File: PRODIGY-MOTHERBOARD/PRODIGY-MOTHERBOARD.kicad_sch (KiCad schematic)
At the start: 0 parts

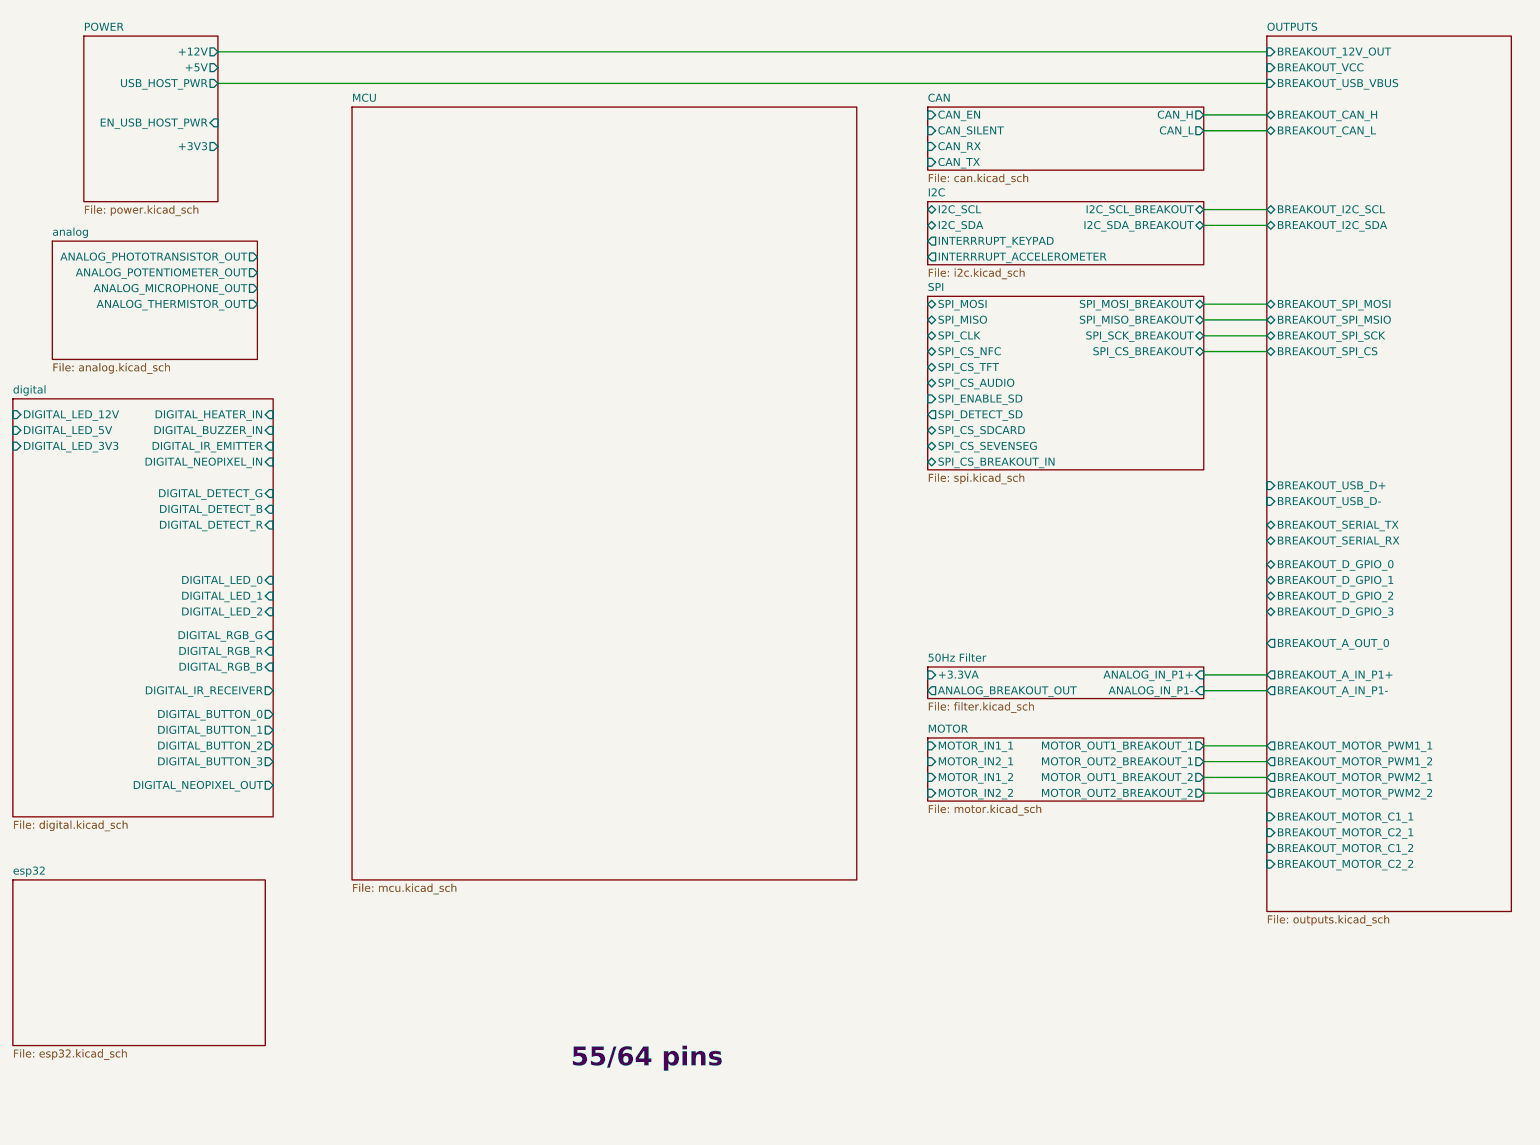
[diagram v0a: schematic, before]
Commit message: 2-axis joystick footprint and sybmbol created. Analog-side done.
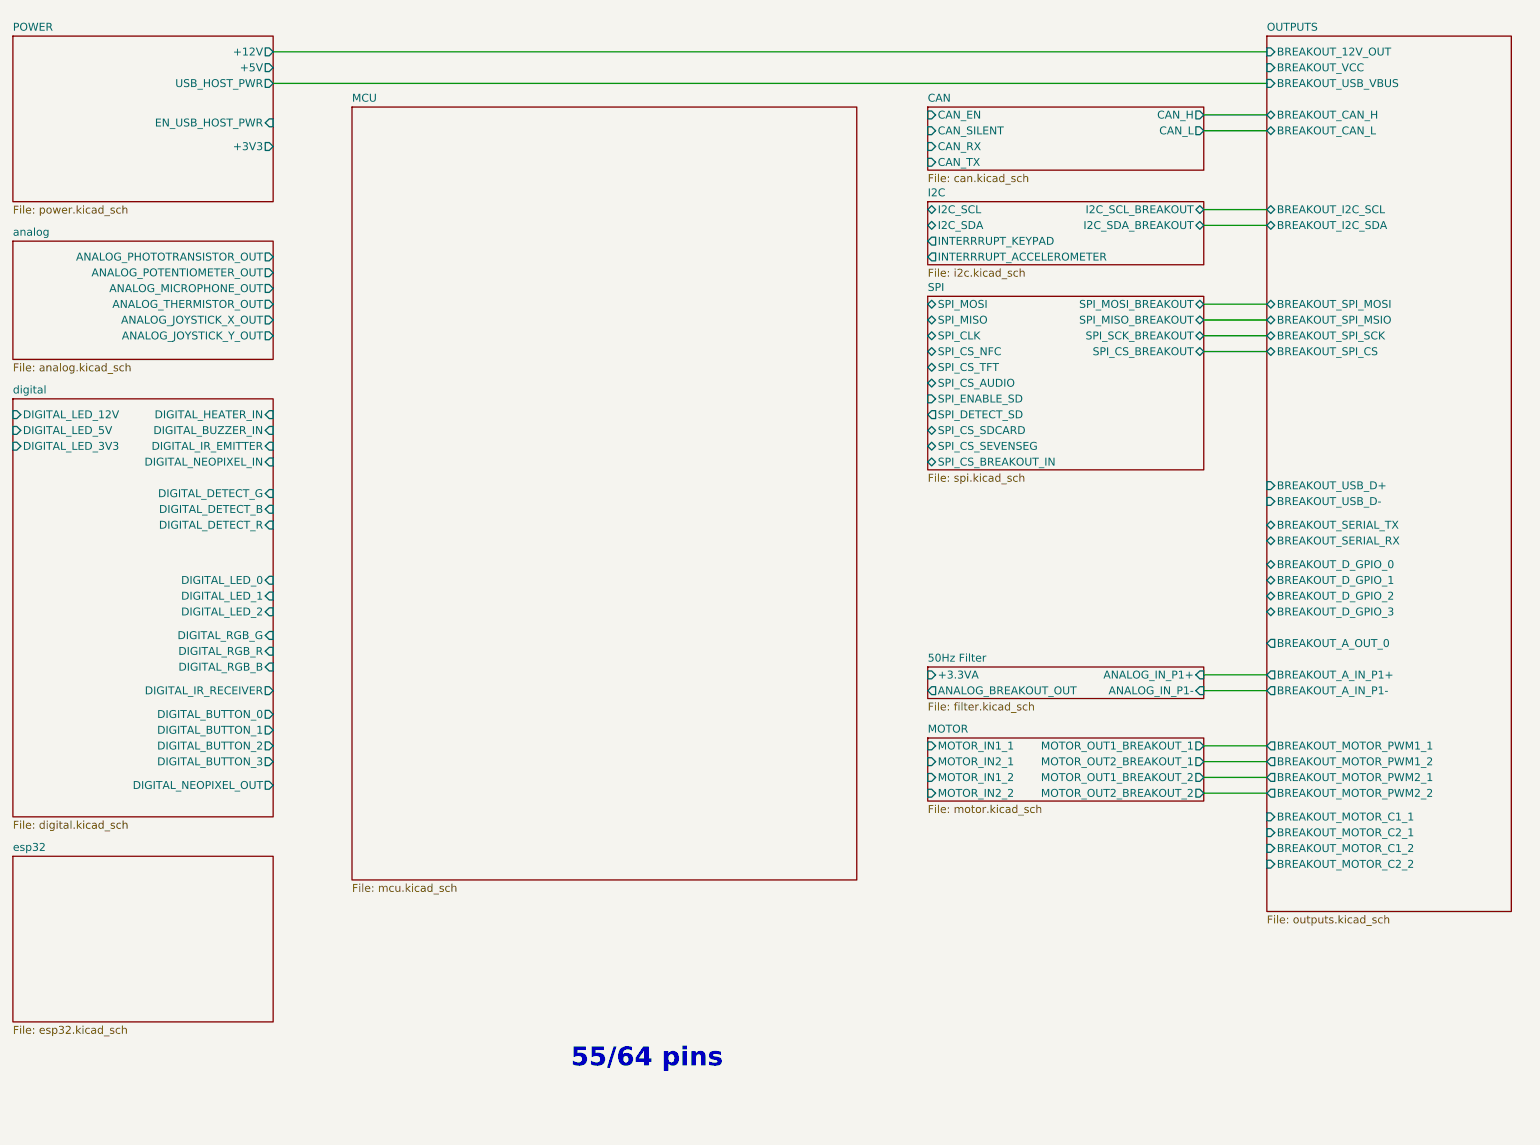
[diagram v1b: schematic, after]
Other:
- sheet analog ports: added ANALOG_JOYSTICK_X_OUT, ANALOG_JOYSTICK_Y_OUT; removed none
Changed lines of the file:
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@@
 	(wire
 		(pts
-			(xy 60.96 21.59) (xy 229.87 21.59)
+			(xy 69.85 21.59) (xy 229.87 21.59)
 		)
 		(stroke
@@
 	(wire
 		(pts
-			(xy 60.96 26.67) (xy 229.87 26.67)
+			(xy 69.85 26.67) (xy 229.87 26.67)
 		)
 		(stroke
@@
 	)
 	(sheet
-		(at 27.94 154.94)
-		(size 40.64 26.67)
+		(at 27.94 151.13)
+		(size 41.91 26.67)
 		(fields_autoplaced yes)
 		(stroke
@@
 		)
 		(property "Sheetname" "esp32"
-			(at 27.94 154.2284 0)
+			(at 27.94 150.4184 0)
 			(effects
 				(font
@@
 		)
 		(property "Sheetfile" "esp32.kicad_sch"
-			(at 27.94 182.1946 0)
+			(at 27.94 178.3846 0)
 			(effects
 				(font
@@
 		)
 		(property "Field2" ""
-			(at 27.94 154.94 0)
+			(at 27.94 151.13 0)
 			(effects
 				(font
@@
 	)
 	(sheet
-		(at 39.37 19.05)
-		(size 21.59 26.67)
+		(at 27.94 19.05)
+		(size 41.91 26.67)
 		(fields_autoplaced yes)
 		(stroke
@@
 		)
 		(property "Sheetname" "POWER"
-			(at 39.37 18.3384 0)
+			(at 27.94 18.3384 0)
 			(effects
 				(font
@@
 		)
 		(property "Sheetfile" "power.kicad_sch"
-			(at 39.37 46.3046 0)
+			(at 27.94 46.3046 0)
 			(effects
 				(font
@@
 		)
 		(pin "+3V3" output
-			(at 60.96 36.83 0)
+			(at 69.85 36.83 0)
 			(effects
 				(font
@@
 		)
 		(pin "+12V" output
-			(at 60.96 21.59 0)
+			(at 69.85 21.59 0)
 			(effects
 				(font
@@
 		)
 		(pin "+5V" output
-			(at 60.96 24.13 0)
+			(at 69.85 24.13 0)
 			(effects
 				(font
@@
 		)
 		(pin "USB_HOST_PWR" output
-			(at 60.96 26.67 0)
+			(at 69.85 26.67 0)
 			(effects
 				(font
@@
 		)
 		(pin "EN_USB_HOST_PWR" input
-			(at 60.96 33.02 0)
+			(at 69.85 33.02 0)
 			(effects
 				(font
@@
 	)
 	(sheet
-		(at 34.29 52.07)
-		(size 33.02 19.05)
+		(at 27.94 52.07)
+		(size 41.91 19.05)
 		(fields_autoplaced yes)
 		(stroke
@@
 		)
 		(property "Sheetname" "analog"
-			(at 34.29 51.3584 0)
+			(at 27.94 51.3584 0)
 			(effects
 				(font
@@
 		)
 		(property "Sheetfile" "analog.kicad_sch"
-			(at 34.29 71.7046 0)
+			(at 27.94 71.7046 0)
 			(effects
 				(font
@@
 		)
 		(property "Field2" ""
-			(at 34.29 52.07 0)
+			(at 27.94 52.07 0)
 			(effects
 				(font
@@
 		)
 		(pin "ANALOG_POTENTIOMETER_OUT" output
-			(at 67.31 57.15 0)
+			(at 69.85 57.15 0)
 			(effects
 				(font
@@
 		)
 		(pin "ANALOG_THERMISTOR_OUT" output
-			(at 67.31 62.23 0)
+			(at 69.85 62.23 0)
 			(effects
 				(font
@@
 		)
 		(pin "ANALOG_PHOTOTRANSISTOR_OUT" output
-			(at 67.31 54.61 0)
+			(at 69.85 54.61 0)
 			(effects
 				(font
@@
 		)
 		(pin "ANALOG_MICROPHONE_OUT" output
-			(at 67.31 59.69 0)
-			(effects
-				(font
+			(at 69.85 59.69 0)
+			(effects
+				(font
+					(size 1.27 1.27)
+				)
+				(justify right)
+			)
+		)
+		(pin "ANALOG_JOYSTICK_X_OUT" output
+			(at 69.85 64.77 0)
+			(effects
+				(font
+					(size 1.27 1.27)
+				)
+				(justify right)
+			)
+		)
+		(pin "ANALOG_JOYSTICK_Y_OUT" output
+			(at 69.85 67.31 0)
+			(effects
+				(font

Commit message: Added pins to MCU. Added Decoder for SPI SS-Multiplexing.
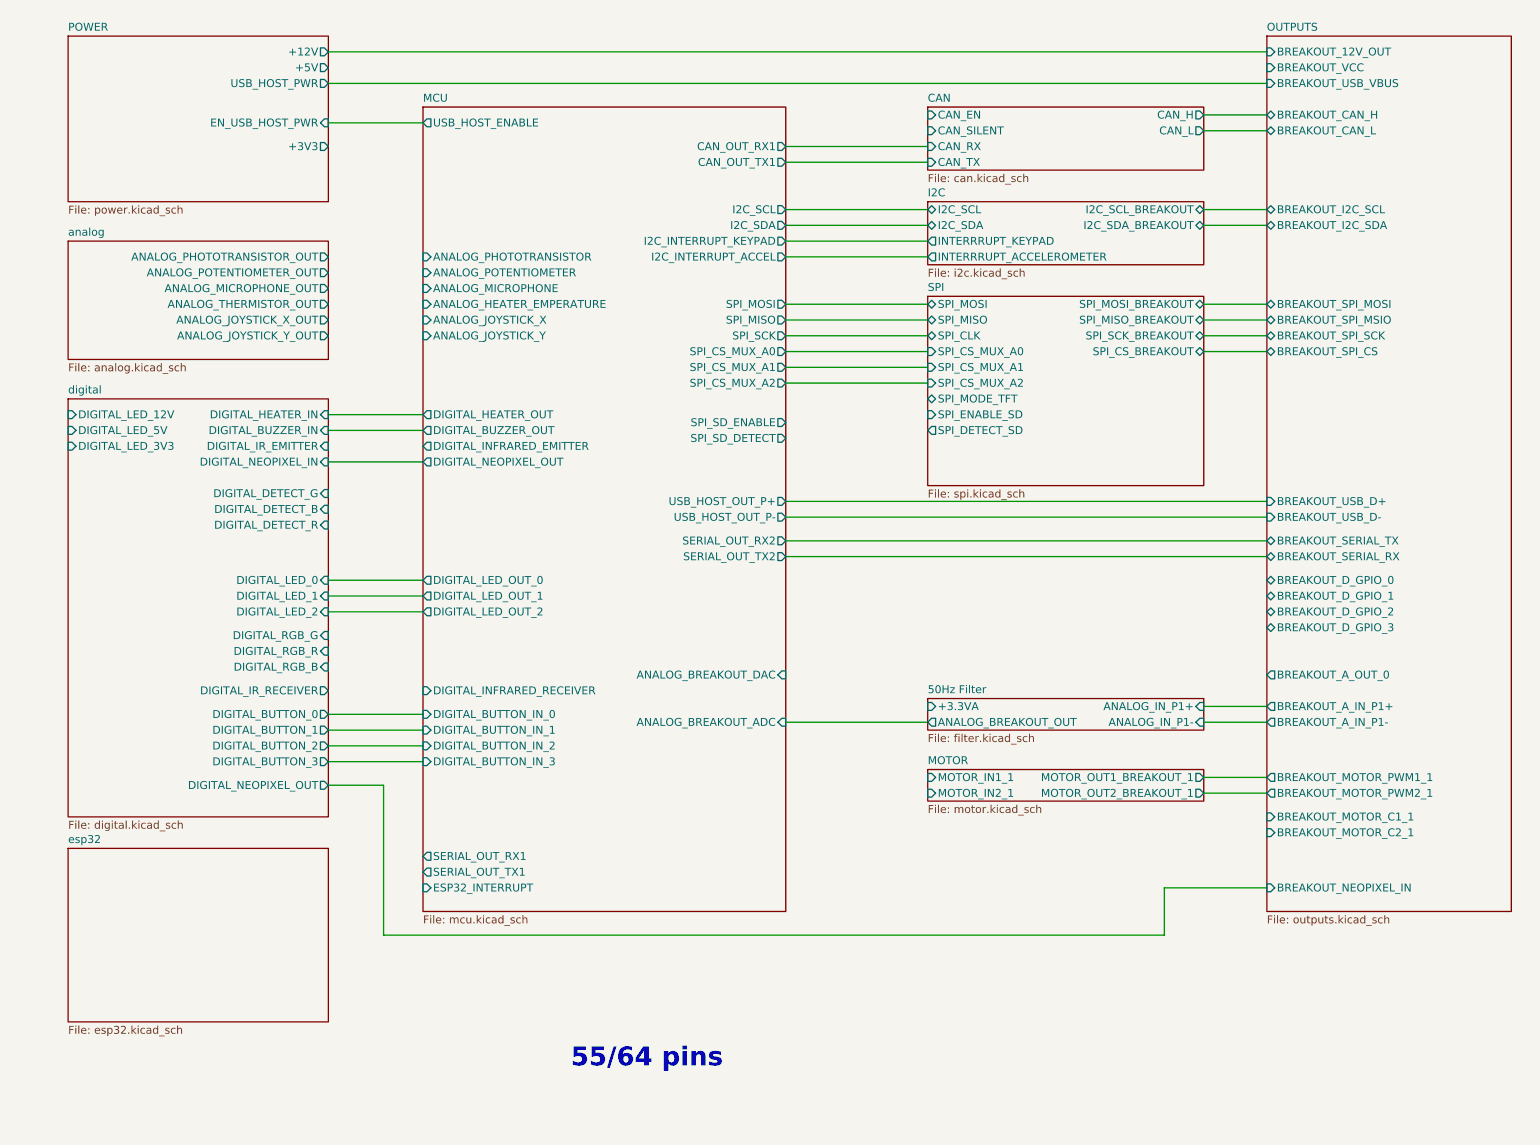
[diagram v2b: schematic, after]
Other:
- sheet MCU ports: added ANALOG_BREAKOUT_ADC, ANALOG_BREAKOUT_DAC, ANALOG_HEATER_EMPERATURE, ANALOG_JOYSTICK_X, ANALOG_JOYSTICK_Y, ANALOG_MICROPHONE, ANALOG_PHOTOTRANSISTOR, ANALOG_POTENTIOMETER, CAN_OUT_RX1, CAN_OUT_TX1, DIGITAL_BUTTON_IN_0, DIGITAL_BUTTON_IN_1, DIGITAL_BUTTON_IN_2, DIGITAL_BUTTON_IN_3, DIGITAL_BUZZER_OUT, DIGITAL_HEATER_OUT, DIGITAL_INFRARED_EMITTER, DIGITAL_INFRARED_RECEIVER, DIGITAL_LED_OUT_0, DIGITAL_LED_OUT_1, DIGITAL_LED_OUT_2, DIGITAL_NEOPIXEL_OUT, ESP32_INTERRUPT, I2C_INTERRUPT_ACCEL, I2C_INTERRUPT_KEYPAD, I2C_SCL, I2C_SDA, SERIAL_OUT_RX1, SERIAL_OUT_RX2, SERIAL_OUT_TX1, SERIAL_OUT_TX2, SPI_CS_MUX_A0, SPI_CS_MUX_A1, SPI_CS_MUX_A2, SPI_MISO, SPI_MOSI, SPI_SCK, SPI_SD_DETECT, SPI_SD_ENABLE, USB_HOST_ENABLE, USB_HOST_OUT_P+, USB_HOST_OUT_P-; removed none
- sheet MOTOR ports: added none; removed MOTOR_IN1_2, MOTOR_IN2_2, MOTOR_OUT1_BREAKOUT_2, MOTOR_OUT2_BREAKOUT_2
- sheet OUTPUTS ports: added BREAKOUT_NEOPIXEL_IN; removed BREAKOUT_MOTOR_C1_2, BREAKOUT_MOTOR_C2_2, BREAKOUT_MOTOR_PWM1_2, BREAKOUT_MOTOR_PWM2_2
- sheet SPI ports: added SPI_CS_MUX_A0, SPI_CS_MUX_A1, SPI_CS_MUX_A2, SPI_MODE_TFT; removed SPI_CS_AUDIO, SPI_CS_BREAKOUT_IN, SPI_CS_NFC, SPI_CS_SDCARD, SPI_CS_SEVENSEG, SPI_CS_TFT

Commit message: Added proper debounce filter elements to buttons.
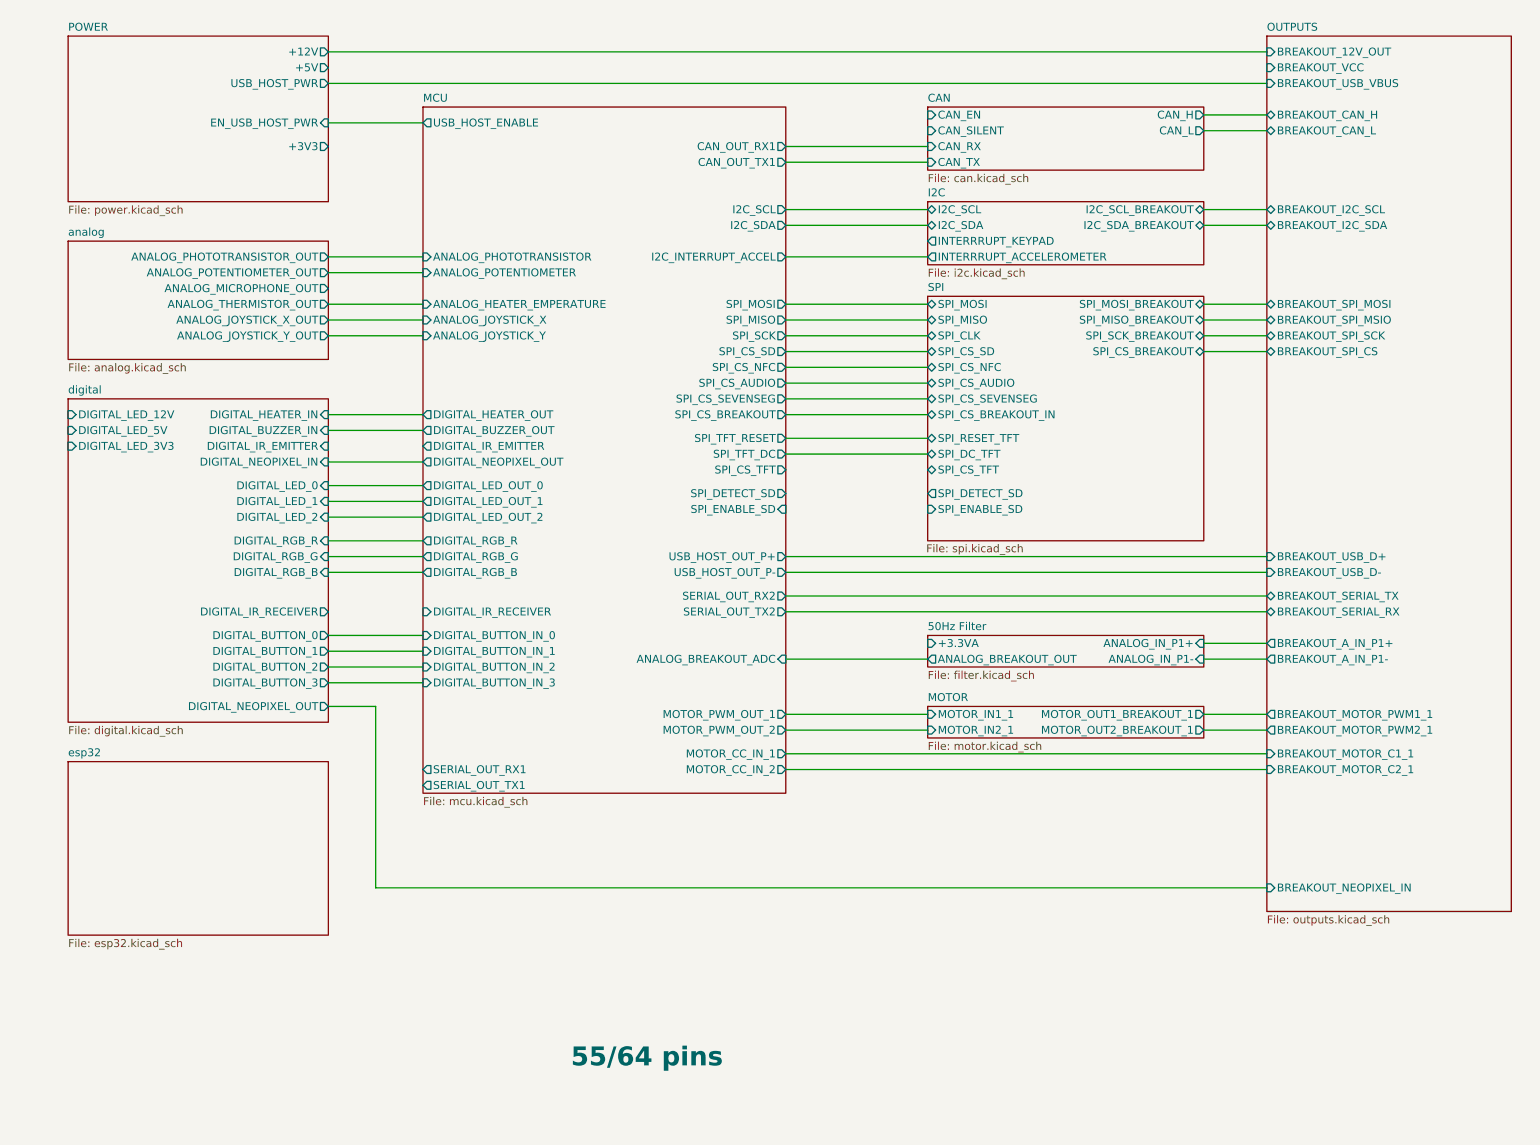
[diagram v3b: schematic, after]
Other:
- sheet MCU ports: added DIGITAL_IR_EMITTER, DIGITAL_IR_RECEIVER, DIGITAL_RGB_B, DIGITAL_RGB_G, DIGITAL_RGB_R, MOTOR_CC_IN_1, MOTOR_CC_IN_2, MOTOR_PWM_OUT_1, MOTOR_PWM_OUT_2, SPI_CS_AUDIO, SPI_CS_BREAKOUT, SPI_CS_NFC, SPI_CS_SD, SPI_CS_SEVENSEG, SPI_CS_TFT, SPI_DETECT_SD, SPI_ENABLE_SD, SPI_TFT_DC, SPI_TFT_RESET; removed ANALOG_BREAKOUT_DAC, ANALOG_MICROPHONE, DIGITAL_INFRARED_EMITTER, DIGITAL_INFRARED_RECEIVER, ESP32_INTERRUPT, I2C_INTERRUPT_KEYPAD, SPI_CS_MUX_A0, SPI_CS_MUX_A1, SPI_CS_MUX_A2, SPI_SD_DETECT, SPI_SD_ENABLE
- sheet OUTPUTS ports: added none; removed BREAKOUT_A_OUT_0, BREAKOUT_D_GPIO_0, BREAKOUT_D_GPIO_1, BREAKOUT_D_GPIO_2, BREAKOUT_D_GPIO_3
- sheet SPI ports: added SPI_CS_AUDIO, SPI_CS_BREAKOUT_IN, SPI_CS_NFC, SPI_CS_SD, SPI_CS_SEVENSEG, SPI_CS_TFT, SPI_DC_TFT, SPI_RESET_TFT; removed SPI_CS_MUX_A0, SPI_CS_MUX_A1, SPI_CS_MUX_A2, SPI_MODE_TFT
- sheet digital ports: added none; removed DIGITAL_DETECT_B, DIGITAL_DETECT_G, DIGITAL_DETECT_R

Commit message: Esp32 motherboard schematic done.
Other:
- sheet esp32 ports: added SERIAL_ESP_RX1, SERIAL_ESP_TX1; removed none
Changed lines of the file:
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@@
 	(wire
 		(pts
-			(xy 86.36 127) (xy 86.36 156.21)
+			(xy 78.74 139.7) (xy 93.98 139.7)
+		)
+		(stroke
+			(width 0)
+			(type default)
+		)
+	)
+	(wire
+		(pts
+			(xy 86.36 127) (xy 86.36 144.78)
 		)
 		(stroke
@@
 	(wire
 		(pts
-			(xy 86.36 156.21) (xy 229.87 156.21)
+			(xy 86.36 144.78) (xy 229.87 144.78)
 		)
 		(stroke
@@
 		(pts
 			(xy 78.74 127) (xy 86.36 127)
+		)
+		(stroke
+			(width 0)
+			(type default)
+		)
+	)
+	(wire
+		(pts
+			(xy 78.74 137.16) (xy 93.98 137.16)
 		)
 		(stroke
@@
 	(sheet
 		(at 36.83 135.89)
-		(size 41.91 27.94)
+		(size 41.91 5.08)
 		(fields_autoplaced yes)
 		(stroke
@@
 		)
 		(property "Sheetfile" "esp32.kicad_sch"
-			(at 36.83 164.4146 0)
+			(at 36.83 141.5546 0)
 			(effects
 				(font
@@
 				)
 				(hide yes)
+			)
+		)
+		(pin "SERIAL_ESP_RX1" input
+			(at 78.74 139.7 0)
+			(effects
+				(font
+					(size 1.27 1.27)
+				)
+				(justify right)
+			)
+		)
+		(pin "SERIAL_ESP_TX1" output
+			(at 78.74 137.16 0)
+			(effects
+				(font
+					(size 1.27 1.27)
+				)
+				(justify right)
 			)
 		)
@@
 		)
 		(pin "BREAKOUT_NEOPIXEL_IN" input
-			(at 229.87 156.21 180)
-			(effects
-				(font
+			(at 229.87 144.78 180)
+			(effects
+				(font
